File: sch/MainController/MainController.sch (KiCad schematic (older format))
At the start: 19 parts, among them J1 Power Input, J2 Sensor_CH1, J3 Sensor_CH2, J4 Sensor_CH3, J5 DIP_SW_IN, J6 Screw_Terminal_01x02, Q1 IRFZ44N, U1 SZH-PWSD-016

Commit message: [PCB] housekeeping
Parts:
- D2: renamed from D?; footprint Diode_THT:D_DO-201AD_P15.24mm_Horizontal -> Diode_THT:D_DO-201AD_P3.81mm_Vertical_AnodeUp
- J2, J3, J4: footprint TerminalBlock_Dinkle2:ECH381V-3p -> TerminalBlock_Dinkle2:ECH381R-3p
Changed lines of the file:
@@
 F 0 "J2" H 8180 3042 50  0000 L CNN
 F 1 "Sensor_CH1" H 8180 2951 50  0000 L CNN
-F 2 "TerminalBlock_Dinkle2:ECH381V-3p" H 8100 3000 50  0001 C CNN
+F 2 "TerminalBlock_Dinkle2:ECH381R-3p" H 8100 3000 50  0001 C CNN
 F 3 "~" H 8100 3000 50  0001 C CNN
 	1    8100 3000
@@
 F 0 "J3" H 8180 3442 50  0000 L CNN
 F 1 "Sensor_CH2" H 8180 3351 50  0000 L CNN
-F 2 "TerminalBlock_Dinkle2:ECH381V-3p" H 8100 3400 50  0001 C CNN
+F 2 "TerminalBlock_Dinkle2:ECH381R-3p" H 8100 3400 50  0001 C CNN
 F 3 "~" H 8100 3400 50  0001 C CNN
 	1    8100 3400
@@
 F 0 "J4" H 8180 3842 50  0000 L CNN
 F 1 "Sensor_CH3" H 8180 3751 50  0000 L CNN
-F 2 "TerminalBlock_Dinkle2:ECH381V-3p" H 8100 3800 50  0001 C CNN
+F 2 "TerminalBlock_Dinkle2:ECH381R-3p" H 8100 3800 50  0001 C CNN
 F 3 "~" H 8100 3800 50  0001 C CNN
 	1    8100 3800
@@
 Wire Wire Line
 	4950 3200 5050 3200
-Text Label 3850 5200 0    50   ~ 0
-12V_input
 Text Label 3100 5550 2    50   ~ 0
 SIG_OUT
@@
 	1    0    0    -1
 $EndComp
-Wire Wire Line
-	3850 5750 3850 5800
-Wire Wire Line
-	3850 5950 3950 5950
+$Comp
+L Diode:1N4148 D1
+U 1 1 5E1337A2
+P 3400 5900
+F 0 "D1" V 3354 5979 50  0000 L CNN
+F 1 "1N4148" V 3445 5979 50  0000 L CNN
+F 2 "Diode_THT:D_DO-35_SOD27_P7.62mm_Horizontal" H 3400 5725 50  0001 C CNN
+F 3 "https://assets.nexperia.com/documents/data-sheet/1N4148_1N4448.pdf" H 3400 5900 50  0001 C CNN
+	1    3400 5900
+	0    1    1    0
+$EndComp
+Wire Wire Line
+	3400 5550 3400 5750
+Wire Wire Line
+	3100 5550 3400 5550
+Wire Wire Line
+	3400 5550 3550 5550
+Connection ~ 3400 5550
+Wire Wire Line
+	3400 6100 3400 6050
+$Comp
+L power:GND #PWR0106
+U 1 1 5E139C42
+P 3400 6100
+F 0 "#PWR0106" H 3400 5850 50  0001 C CNN
+F 1 "GND" H 3405 5927 50  0000 C CNN
+F 2 "" H 3400 6100 50  0001 C CNN
+F 3 "" H 3400 6100 50  0001 C CNN
+	1    3400 6100
+	1    0    0    -1
+$EndComp
+Wire Wire Line
+	4450 5700 4450 5800
+$Comp
+L Diode:1N5822 D2
+U 1 1 5E1D0529
+P 4450 5550
+F 0 "D2" V 4404 5629 50  0000 L CNN
+F 1 "1N5822" V 4495 5629 50  0000 L CNN
+F 2 "Diode_THT:D_DO-201AD_P3.81mm_Vertical_AnodeUp" H 4450 5375 50  0001 C CNN
+F 3 "http://www.vishay.com/docs/88526/1n5820.pdf" H 4450 5550 50  0001 C CNN
+	1    4450 5550
+	0    1    1    0
+$EndComp
+$Comp
+L power:GND #PWR0107
+U 1 1 5E13D445
+P 3850 6100
+F 0 "#PWR0107" H 3850 5850 50  0001 C CNN
+F 1 "GND" H 3855 5927 50  0000 C CNN
+F 2 "" H 3850 6100 50  0001 C CNN
+F 3 "" H 3850 6100 50  0001 C CNN
+	1    3850 6100
+	1    0    0    -1
+$EndComp
+Text Label 3850 5200 0    50   ~ 0
+12V_input
+Wire Wire Line
+	4450 5400 4450 5300
+Wire Wire Line
+	3850 5300 3850 5350
+Wire Wire Line
+	3850 5200 3850 5300
+Connection ~ 3850 5300
+Wire Wire Line
+	4450 5300 3850 5300
+Wire Wire Line
+	3850 6100 3850 6050
+Wire Wire Line
+	3850 6050 3950 6050
 $Comp
 L Connector:Screw_Terminal_01x02 J6
@@
 	1    0    0    -1
 $EndComp
-$Comp
-L Diode:1N4148 D1
-U 1 1 5E1337A2
-P 3400 5900
-F 0 "D1" V 3354 5979 50  0000 L CNN
-F 1 "1N4148" V 3445 5979 50  0000 L CNN
-F 2 "Diode_THT:D_DO-35_SOD27_P7.62mm_Horizontal" H 3400 5725 50  0001 C CNN
-F 3 "https://assets.nexperia.com/documents/data-sheet/1N4148_1N4448.pdf" H 3400 5900 50  0001 C CNN
-	1    3400 5900
-	0    1    1    0
-$EndComp
-Wire Wire Line
-	3400 5550 3400 5750
-Wire Wire Line
-	3100 5550 3400 5550
-Wire Wire Line
-	3400 5550 3550 5550
-Connection ~ 3400 5550
-Wire Wire Line
-	3400 6100 3400 6050
-$Comp
-L power:GND #PWR0106
-U 1 1 5E139C42
-P 3400 6100
-F 0 "#PWR0106" H 3400 5850 50  0001 C CNN
-F 1 "GND" H 3405 5927 50  0000 C CNN
-F 2 "" H 3400 6100 50  0001 C CNN
-F 3 "" H 3400 6100 50  0001 C CNN
-	1    3400 6100
-	1    0    0    -1
-$EndComp
-Wire Wire Line
-	3850 6100 3850 6050
-$Comp
-L power:GND #PWR0107
-U 1 1 5E13D445
-P 3850 6100
-F 0 "#PWR0107" H 3850 5850 50  0001 C CNN
-F 1 "GND" H 3855 5927 50  0000 C CNN
-F 2 "" H 3850 6100 50  0001 C CNN
-F 3 "" H 3850 6100 50  0001 C CNN
-	1    3850 6100
-	1    0    0    -1
-$EndComp
-Wire Wire Line
-	3850 6050 3950 6050
-Wire Wire Line
-	3850 5200 3850 5300
+Wire Wire Line
+	3850 5950 3950 5950
+Wire Wire Line
+	3850 5800 3850 5950
+Wire Wire Line
+	3850 5750 3850 5800
+Connection ~ 3850 5800
 Wire Wire Line
 	4450 5800 3850 5800
-Connection ~ 3850 5800
-Wire Wire Line
-	3850 5800 3850 5950
-Wire Wire Line
-	4450 5300 3850 5300
-Connection ~ 3850 5300
-Wire Wire Line
-	3850 5300 3850 5350
-$Comp
-L Diode:1N5822 D?
-U 1 1 5E1D0529
-P 4450 5550
-F 0 "D?" V 4404 5629 50  0000 L CNN
-F 1 "1N5822" V 4495 5629 50  0000 L CNN
-F 2 "Diode_THT:D_DO-201AD_P15.24mm_Horizontal" H 4450 5375 50  0001 C CNN
-F 3 "http://www.vishay.com/docs/88526/1n5820.pdf" H 4450 5550 50  0001 C CNN
-	1    4450 5550
-	0    1    1    0
-$EndComp
-Wire Wire Line
-	4450 5700 4450 5800
-Wire Wire Line
-	4450 5400 4450 5300
 $EndSCHEMATC

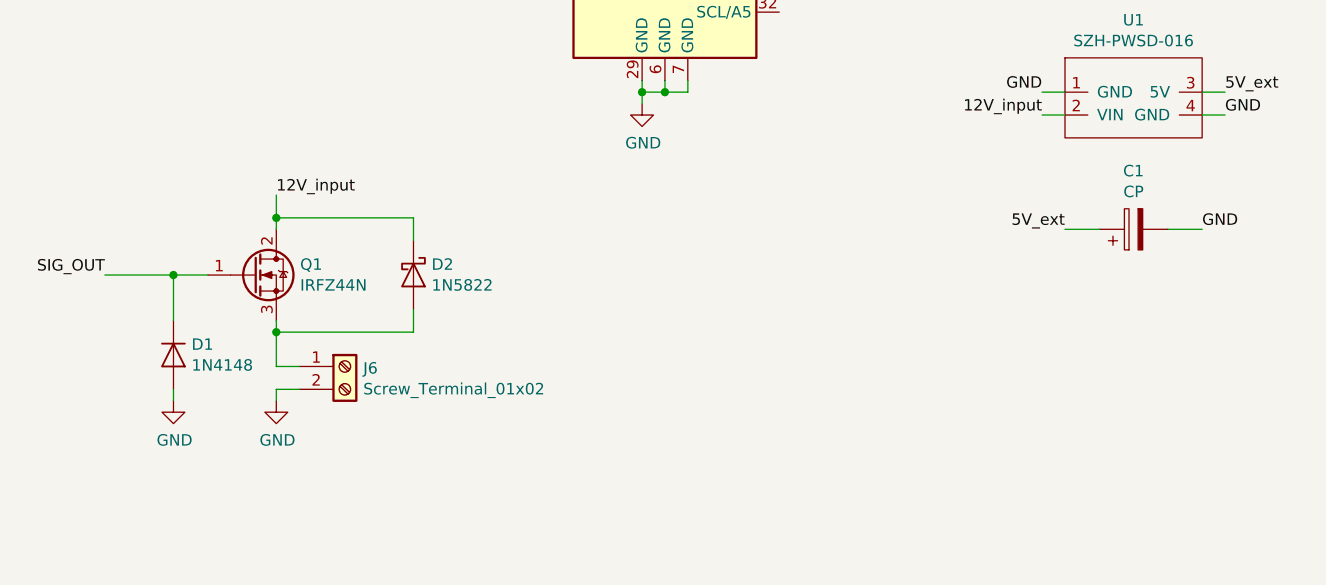
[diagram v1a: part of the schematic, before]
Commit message: [pcb] update pcb pattern
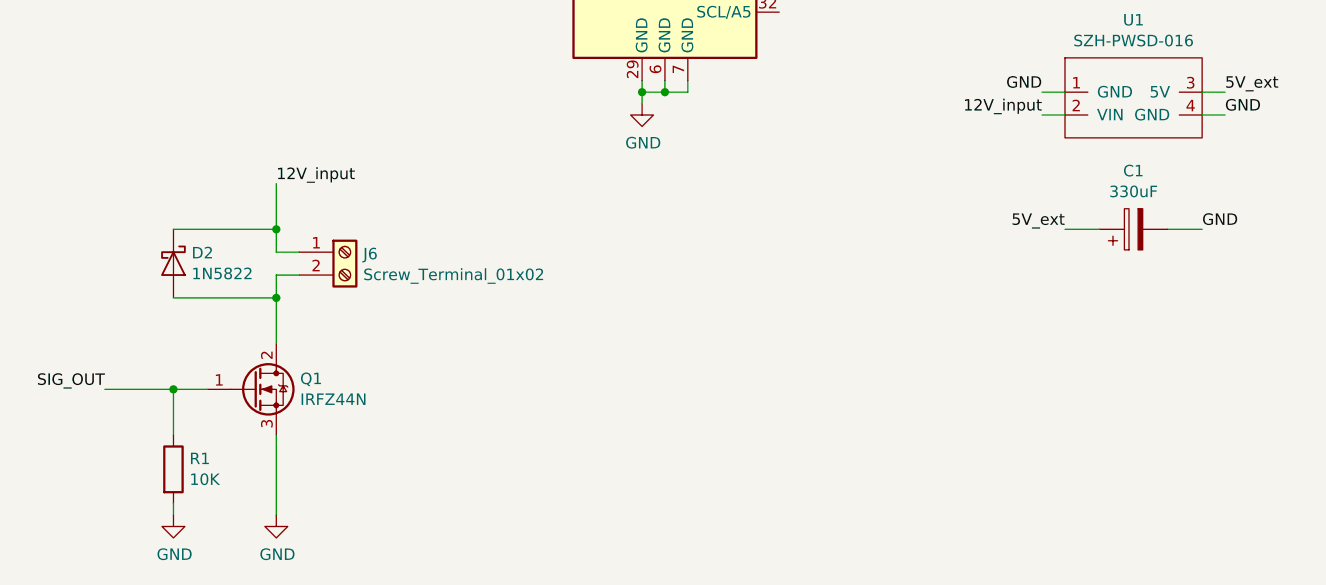
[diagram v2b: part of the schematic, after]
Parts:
- removed D1: 1N4148, Diode_THT:D_DO-35_SOD27_P7.62mm_Horizontal, symbol Diode:1N4148
- added R1: 10K, Resistor_SMD:R_1806_4516Metric_Pad1.57x1.80mm_HandSolder, symbol Device:R
- C1: value CP -> 330uF
- D2: footprint Diode_THT:D_DO-201AD_P3.81mm_Vertical_AnodeUp -> Diode_THT:D_DO-201AD_P5.08mm_Vertical_KathodeUp
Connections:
- net 12V_input: now also J6.1 (Pin_1); no longer Q1.2 (D)
- net GND: now also Q1.3 (S), R1.2; no longer J6.2 (Pin_2)
- net SIG_OUT: now also R1.1
- new net: D2.2 (A), J6.2 (Pin_2), Q1.2 (D)
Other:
- moved on the sheet: D2, J6, Q1
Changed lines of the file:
@@
 P 7600 5350
 F 0 "C1" V 7855 5350 50  0000 C CNN
-F 1 "CP" V 7764 5350 50  0000 C CNN
+F 1 "330uF" V 7764 5350 50  0000 C CNN
 F 2 "Capacitor_THT:CP_Radial_D8.0mm_P3.80mm" H 7638 5200 50  0001 C CNN
 F 3 "~" H 7600 5350 50  0001 C CNN
@@
 Wire Wire Line
 	4950 3200 5050 3200
-Text Label 3100 5550 2    50   ~ 0
+Text Label 3100 6050 2    50   ~ 0
 SIG_OUT
 $Comp
 L Transistor_FET:IRF3205 Q1
 U 1 1 5E1544B4
-P 3750 5550
-F 0 "Q1" H 3954 5596 50  0000 L CNN
-F 1 "IRFZ44N" H 3954 5505 50  0000 L CNN
-F 2 "Package_TO_SOT_THT:TO-220-3_Vertical" H 4000 5475 50  0001 L CIN
-F 3 "http://www.irf.com/product-info/datasheets/data/irf3205.pdf" H 3750 5550 50  0001 L CNN
-	1    3750 5550
+P 3750 6050
+F 0 "Q1" H 3954 6096 50  0000 L CNN
+F 1 "IRFZ44N" H 3954 6005 50  0000 L CNN
+F 2 "Package_TO_SOT_THT:TO-220-3_Vertical" H 4000 5975 50  0001 L CIN
+F 3 "http://www.irf.com/product-info/datasheets/data/irf3205.pdf" H 3750 6050 50  0001 L CNN
+	1    3750 6050
 	1    0    0    -1
 $EndComp
-$Comp
-L Diode:1N4148 D1
-U 1 1 5E1337A2
-P 3400 5900
-F 0 "D1" V 3354 5979 50  0000 L CNN
-F 1 "1N4148" V 3445 5979 50  0000 L CNN
-F 2 "Diode_THT:D_DO-35_SOD27_P7.62mm_Horizontal" H 3400 5725 50  0001 C CNN
-F 3 "https://assets.nexperia.com/documents/data-sheet/1N4148_1N4448.pdf" H 3400 5900 50  0001 C CNN
-	1    3400 5900
-	0    1    1    0
-$EndComp
 Wire Wire Line
-	3400 5550 3400 5750
+	3400 6050 3400 6250
 Wire Wire Line
-	3100 5550 3400 5550
+	3100 6050 3400 6050
 Wire Wire Line
-	3400 5550 3550 5550
-Connection ~ 3400 5550
+	3400 6050 3550 6050
+Connection ~ 3400 6050
 Wire Wire Line
-	3400 6100 3400 6050
+	3400 6600 3400 6550
 $Comp
 L power:GND #PWR0106
 U 1 1 5E139C42
-P 3400 6100
-F 0 "#PWR0106" H 3400 5850 50  0001 C CNN
-F 1 "GND" H 3405 5927 50  0000 C CNN
-F 2 "" H 3400 6100 50  0001 C CNN
-F 3 "" H 3400 6100 50  0001 C CNN
-	1    3400 6100
+P 3400 6600
+F 0 "#PWR0106" H 3400 6350 50  0001 C CNN
+F 1 "GND" H 3405 6427 50  0000 C CNN
+F 2 "" H 3400 6600 50  0001 C CNN
+F 3 "" H 3400 6600 50  0001 C CNN
+	1    3400 6600
 	1    0    0    -1
-$EndComp
-Wire Wire Line
-	4450 5700 4450 5800
-$Comp
-L Diode:1N5822 D2
-U 1 1 5E1D0529
-P 4450 5550
-F 0 "D2" V 4404 5629 50  0000 L CNN
-F 1 "1N5822" V 4495 5629 50  0000 L CNN
-F 2 "Diode_THT:D_DO-201AD_P3.81mm_Vertical_AnodeUp" H 4450 5375 50  0001 C CNN
-F 3 "http://www.vishay.com/docs/88526/1n5820.pdf" H 4450 5550 50  0001 C CNN
-	1    4450 5550
-	0    1    1    0
 $EndComp
 $Comp
 L power:GND #PWR0107
 U 1 1 5E13D445
-P 3850 6100
-F 0 "#PWR0107" H 3850 5850 50  0001 C CNN
-F 1 "GND" H 3855 5927 50  0000 C CNN
-F 2 "" H 3850 6100 50  0001 C CNN
-F 3 "" H 3850 6100 50  0001 C CNN
-	1    3850 6100
+P 3850 6600
+F 0 "#PWR0107" H 3850 6350 50  0001 C CNN
+F 1 "GND" H 3855 6427 50  0000 C CNN
+F 2 "" H 3850 6600 50  0001 C CNN
+F 3 "" H 3850 6600 50  0001 C CNN
+	1    3850 6600
 	1    0    0    -1
 $EndComp
-Text Label 3850 5200 0    50   ~ 0
+Text Label 3850 5150 0    50   ~ 0
 12V_input
-Wire Wire Line
-	4450 5400 4450 5300
-Wire Wire Line
-	3850 5300 3850 5350
-Wire Wire Line
-	3850 5200 3850 5300
-Connection ~ 3850 5300
-Wire Wire Line
-	4450 5300 3850 5300
-Wire Wire Line
-	3850 6100 3850 6050
-Wire Wire Line
-	3850 6050 3950 6050
 $Comp
 L Connector:Screw_Terminal_01x02 J6
 U 1 1 5E1699D6
-P 4150 5950
-F 0 "J6" H 4230 5942 50  0000 L CNN
-F 1 "Screw_Terminal_01x02" H 4230 5851 50  0000 L CNN
-F 2 "TerminalBlock_Dinkle2:ECH381V-2p" H 4150 5950 50  0001 C CNN
-F 3 "~" H 4150 5950 50  0001 C CNN
-	1    4150 5950
+P 4150 5450
+F 0 "J6" H 4230 5442 50  0000 L CNN
+F 1 "Screw_Terminal_01x02" H 4230 5351 50  0000 L CNN
+F 2 "TerminalBlock_Dinkle2:ECH381V-2p" H 4150 5450 50  0001 C CNN
+F 3 "~" H 4150 5450 50  0001 C CNN
+	1    4150 5450
 	1    0    0    -1
 $EndComp
 Wire Wire Line
-	3850 5950 3950 5950
+	3850 5450 3950 5450
 Wire Wire Line
-	3850 5800 3850 5950
+	3850 5550 3950 5550
+$Comp
+L Device:R R1
+U 1 1 5E2817C0
+P 3400 6400
+F 0 "R1" H 3470 6446 50  0000 L CNN
+F 1 "10K" H 3470 6355 50  0000 L CNN
+F 2 "Resistor_SMD:R_1806_4516Metric_Pad1.57x1.80mm_HandSolder" V 3330 6400 50  0001 C CNN
+F 3 "~" H 3400 6400 50  0001 C CNN
+	1    3400 6400
+	1    0    0    -1
+$EndComp
 Wire Wire Line
-	3850 5750 3850 5800
-Connection ~ 3850 5800
+	3850 5550 3850 5650
 Wire Wire Line
-	4450 5800 3850 5800
+	3850 6250 3850 6600
+Wire Wire Line
+	3850 5350 3400 5350
+Wire Wire Line
+	3400 5650 3850 5650
+Connection ~ 3850 5650
+Wire Wire Line
+	3850 5650 3850 5850
+Connection ~ 3850 5350
+Wire Wire Line
+	3850 5350 3850 5450
+Wire Wire Line
+	3850 5150 3850 5350
+$Comp
+L Diode:1N5822 D2
+U 1 1 5E1D0529
+P 3400 5500
+F 0 "D2" V 3354 5579 50  0000 L CNN
+F 1 "1N5822" V 3445 5579 50  0000 L CNN
+F 2 "Diode_THT:D_DO-201AD_P5.08mm_Vertical_KathodeUp" H 3400 5325 50  0001 C CNN
+F 3 "http://www.vishay.com/docs/88526/1n5820.pdf" H 3400 5500 50  0001 C CNN
+	1    3400 5500
+	0    1    1    0
+$EndComp
 $EndSCHEMATC

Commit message: [pcb] fix tr control circuit and update pcb layout
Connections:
- net 12V_input: no longer D2.1 (K)
- net GND: now also D2.2 (A)
- net at J6.2 (Pin_2), Q1.2 (D): now also D2.1 (K); no longer D2.2 (A)
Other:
- moved on the sheet: D2
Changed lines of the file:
@@
 $EndComp
 Wire Wire Line
-	3850 5550 3850 5650
-Wire Wire Line
-	3850 6250 3850 6600
-Wire Wire Line
-	3850 5350 3400 5350
-Wire Wire Line
-	3400 5650 3850 5650
-Connection ~ 3850 5650
-Wire Wire Line
-	3850 5650 3850 5850
-Connection ~ 3850 5350
-Wire Wire Line
-	3850 5350 3850 5450
-Wire Wire Line
-	3850 5150 3850 5350
+	3850 6250 3850 6300
 $Comp
 L Diode:1N5822 D2
 U 1 1 5E1D0529
-P 3400 5500
-F 0 "D2" V 3354 5579 50  0000 L CNN
-F 1 "1N5822" V 3445 5579 50  0000 L CNN
-F 2 "Diode_THT:D_DO-201AD_P5.08mm_Vertical_KathodeUp" H 3400 5325 50  0001 C CNN
-F 3 "http://www.vishay.com/docs/88526/1n5820.pdf" H 3400 5500 50  0001 C CNN
-	1    3400 5500
+P 4400 6050
+F 0 "D2" V 4354 6129 50  0000 L CNN
+F 1 "1N5822" V 4445 6129 50  0000 L CNN
+F 2 "Diode_THT:D_DO-201AD_P5.08mm_Vertical_KathodeUp" H 4400 5875 50  0001 C CNN
+F 3 "http://www.vishay.com/docs/88526/1n5820.pdf" H 4400 6050 50  0001 C CNN
+	1    4400 6050
 	0    1    1    0
 $EndComp
+Wire Wire Line
+	3850 5550 3850 5800
+Wire Wire Line
+	3850 5150 3850 5450
+Wire Wire Line
+	4400 5900 4400 5800
+Wire Wire Line
+	4400 5800 3850 5800
+Connection ~ 3850 5800
+Wire Wire Line
+	3850 5800 3850 5850
+Wire Wire Line
+	4400 6200 4400 6300
+Wire Wire Line
+	4400 6300 3850 6300
+Connection ~ 3850 6300
+Wire Wire Line
+	3850 6300 3850 6600
 $EndSCHEMATC
